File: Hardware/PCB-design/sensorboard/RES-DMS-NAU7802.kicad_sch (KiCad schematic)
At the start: 43 parts, among them J1 Conn_01x06, J2 straingauge, J4 straingauge, J5 straingauge, J6 straingauge, U1 NAU7802-SGI

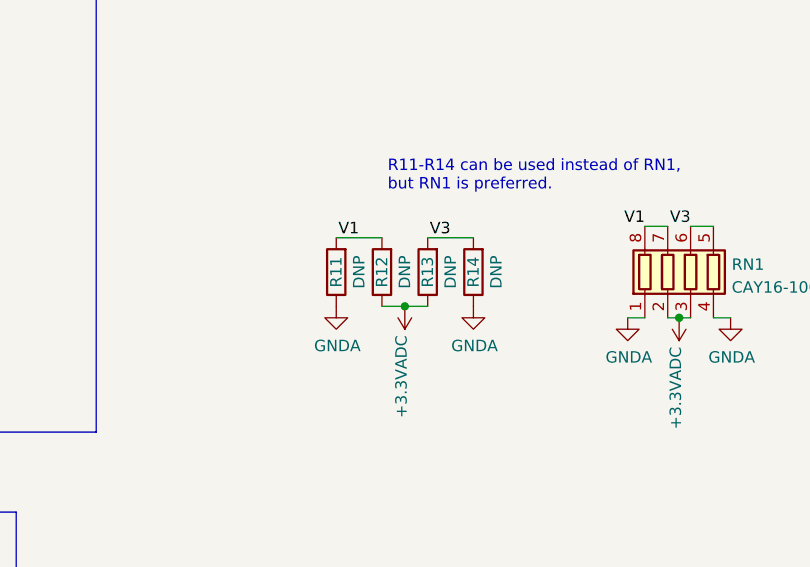
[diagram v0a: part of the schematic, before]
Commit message: Updated schematic/PCB (values for R-Net or alternatives), updated iBOM
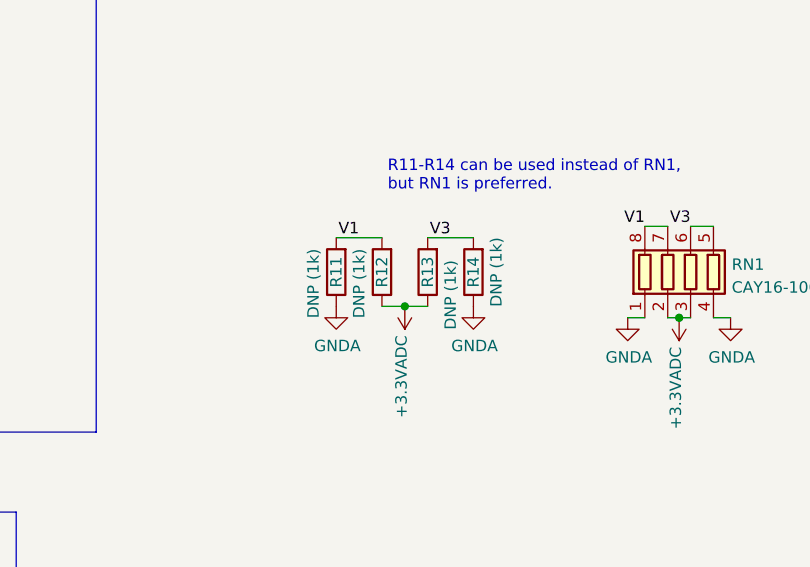
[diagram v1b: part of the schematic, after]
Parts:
- R11, R12, R13, R14: value DNP -> DNP (1k)
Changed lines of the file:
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@@
     (in_bom yes) (on_board yes)
     (property "Reference" "R14" (id 0) (at 176.53 107.95 90))
-    (property "Value" "DNP" (id 1) (at 179.07 107.95 90))
+    (property "Value" "DNP (1k)" (id 1) (at 179.07 107.95 90))
     (property "Footprint" "Resistor_SMD:R_1206_3216Metric" (id 2) (at 178.308 107.95 90)
       (effects (font (size 1.27 1.27)) hide)
@@
     (in_bom yes) (on_board yes)
     (property "Reference" "R13" (id 0) (at 171.45 107.95 90))
-    (property "Value" "DNP" (id 1) (at 173.99 107.95 90))
+    (property "Value" "DNP (1k)" (id 1) (at 173.99 110.49 90))
     (property "Footprint" "Resistor_SMD:R_1206_3216Metric" (id 2) (at 173.228 107.95 90)
       (effects (font (size 1.27 1.27)) hide)
@@
     (in_bom yes) (on_board yes)
     (property "Reference" "R11" (id 0) (at 161.29 107.95 90))
-    (property "Value" "DNP" (id 1) (at 163.83 107.95 90))
+    (property "Value" "DNP (1k)" (id 1) (at 158.75 109.22 90))
     (property "Footprint" "Resistor_SMD:R_1206_3216Metric" (id 2) (at 163.068 107.95 90)
       (effects (font (size 1.27 1.27)) hide)
@@
     (in_bom yes) (on_board yes)
     (property "Reference" "R12" (id 0) (at 166.37 107.95 90))
-    (property "Value" "DNP" (id 1) (at 168.91 107.95 90))
+    (property "Value" "DNP (1k)" (id 1) (at 163.83 109.22 90))
     (property "Footprint" "Resistor_SMD:R_1206_3216Metric" (id 2) (at 168.148 107.95 90)
       (effects (font (size 1.27 1.27)) hide)
@@
     )
     (path "/75bc358e-cfd4-4683-9983-e89c2e96b124"
-      (reference "R11") (unit 1) (value "DNP") (footprint "Resistor_SMD:R_1206_3216Metric")
+      (reference "R11") (unit 1) (value "DNP (1k)") (footprint "Resistor_SMD:R_1206_3216Metric")
     )
     (path "/b50bcc1f-0c0c-4c40-9ffe-e9cc6a509b9e"
-      (reference "R12") (unit 1) (value "DNP") (footprint "Resistor_SMD:R_1206_3216Metric")
+      (reference "R12") (unit 1) (value "DNP (1k)") (footprint "Resistor_SMD:R_1206_3216Metric")
     )
     (path "/1c410388-6dbc-4d7f-92bb-c866584eba47"
-      (reference "R13") (unit 1) (value "DNP") (footprint "Resistor_SMD:R_1206_3216Metric")
+      (reference "R13") (unit 1) (value "DNP (1k)") (footprint "Resistor_SMD:R_1206_3216Metric")
     )
     (path "/106b48ce-c343-4bc1-a966-95d5a5c1ee63"
-      (reference "R14") (unit 1) (value "DNP") (footprint "Resistor_SMD:R_1206_3216Metric")
+      (reference "R14") (unit 1) (value "DNP (1k)") (footprint "Resistor_SMD:R_1206_3216Metric")
     )
     (path "/e585351b-5699-4104-99ac-e99731ac32b5"
